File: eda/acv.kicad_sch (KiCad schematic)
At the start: 0 parts

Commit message: Add OBD2 connector symbol and footprint
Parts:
- added J1: ~, symbol acv:OBD2_J1962_MALE_90
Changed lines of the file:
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@@
 	(generator_version "9.0")
 	(paper "A4")
+	(symbol
+		(lib_id "acv:OBD2_J1962_MALE_90")
+		(at 88.9 63.5 0)
+		(unit 1)
+		(exclude_from_sim no)
+		(in_bom yes)
+		(on_board yes)
+		(dnp no)
+		(fields_autoplaced yes)
+		(property "Reference" "J1"
+			(at 107.95 63.4999 0)
+			(effects
+				(font
+					(size 1.27 1.27)
+				)
+				(justify left)
+			)
+		)
+		(property "Value" "~"
+			(at 107.95 66.0399 0)
+			(effects
+				(font
+					(size 1.27 1.27)
+				)
+				(justify left)
+			)
+		)
+		(property "Footprint" ""
+			(at 88.9 63.5 0)
+			(effects
+				(font
+					(size 1.27 1.27)
+				)
+				(hide yes)
+			)
+		)
+		(property "Datasheet" ""
+			(at 88.9 63.5 0)
+			(effects
+				(font
+					(size 1.27 1.27)
+				)
+				(hide yes)
+			)
+		)
+		(property "Description" ""
+			(at 88.9 63.5 0)
+			(effects
+				(font
+					(size 1.27 1.27)
+				)
+				(hide yes)
+			)
+		)
+		(pin "16"
+		)
+		(pin "9"
+		)
+		(pin "10"
+		)
+		(pin "15"
+		)
+		(pin "7"
+		)
+		(pin "6"
+		)
+		(pin "13"
+		)
+		(pin "5"
+		)
+		(pin "14"
+		)
+		(pin "12"
+		)
+		(pin "8"
+		)
+		(pin "4"
+		)
+		(pin "3"
+		)
+		(pin "11"
+		)
+		(pin "2"
+		)
+		(pin "1"
+		)
+		(instances
+			(project ""
+				(path "/b2ca9fb0-a35f-4499-b995-6512249a25c5"
+					(reference "J1")
+					(unit 1)
+				)
+			)
+		)
+	)
 	(sheet_instances
 		(path "/"

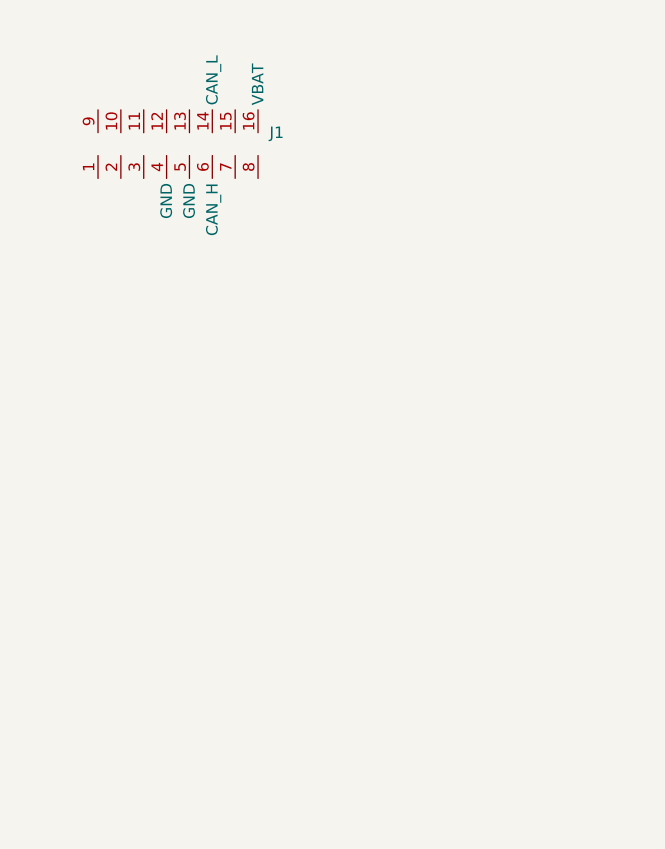
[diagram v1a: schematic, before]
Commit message: Add CAN transceiver symbol and footprint
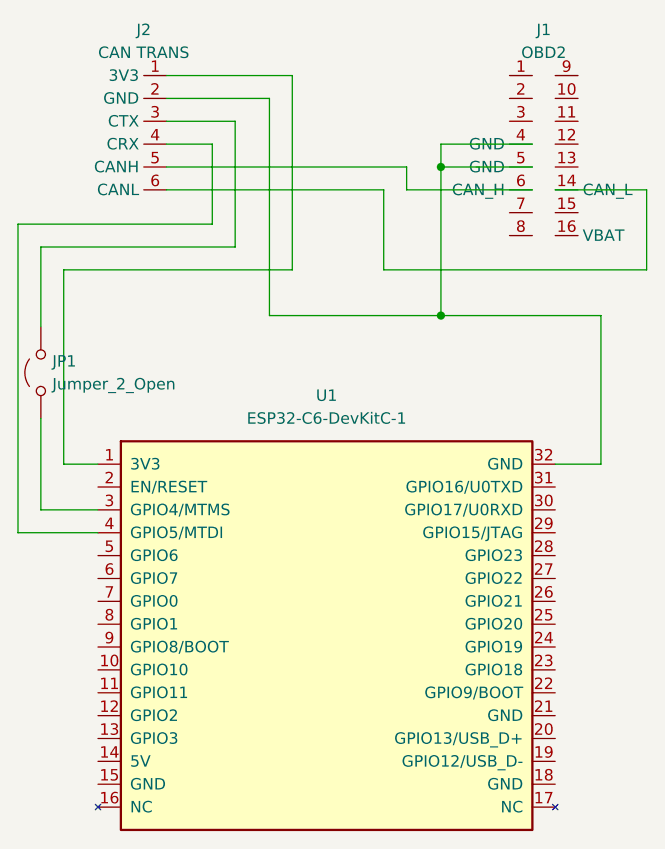
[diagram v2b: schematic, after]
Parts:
- added J2: CAN TRANS, symbol acv:SN65HVD230
- added JP1: Jumper_2_Open, symbol Jumper:Jumper_2_Open
- added U1: ESP32-C6-DevKitC-1, PCM_Espressif:ESP32-C6-DevKitC-1, symbol Espressif:ESP32-C6-DevKitC-1
- J1: value ~ -> OBD2
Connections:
- net at J1.14 (CAN_L): now also J2.6 (CANL)
- net at J1.4 (GND): now also J1.5 (GND), J2.2 (GND), U1.32 (GND)
- net at J1.6 (CAN_H): now also J2.5 (CANH)
- new net: J2.1 (3V3), U1.1 (3V3)
- new net: J2.3 (CTX), JP1.2 (B)
- new net: J2.4 (CRX), U1.4 (GPIO5/MTDI)
- new net: JP1.1 (A), U1.3 (GPIO4/MTMS)
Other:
- moved on the sheet: J1

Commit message: Add led and twai backend tasks
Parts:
- added D1: BLUE LED, symbol Device:LED
- added R1: 330ohm, symbol Device:R
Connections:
- net at J2.1 (3V3), U1.1 (3V3): now also R1.1
- net at U1.28 (GPIO23): now also D1.1 (K)
- new net: D1.2 (A), R1.2
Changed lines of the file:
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@@
 	(paper "A4")
+	(junction
+		(at 104.14 78.74)
+		(diameter 0)
+		(color 0 0 0 0)
+	)
 	(junction
 		(at 127 83.82)
@@
 	(wire
 		(pts
+			(xy 152.4 86.36) (xy 152.4 92.71)
+		)
+		(stroke
+			(width 0)
+			(type default)
+		)
+	)
+	(wire
+		(pts
 			(xy 139.7 100.33) (xy 144.78 100.33)
 		)
@@
 	(wire
 		(pts
+			(xy 139.7 110.49) (xy 152.4 110.49)
+		)
+		(stroke
+			(width 0)
+			(type default)
+		)
+	)
+	(wire
+		(pts
 			(xy 144.78 100.33) (xy 144.78 83.82)
 		)
@@
 	(wire
 		(pts
+			(xy 152.4 100.33) (xy 152.4 102.87)
+		)
+		(stroke
+			(width 0)
+			(type default)
+		)
+	)
+	(wire
+		(pts
 			(xy 137.16 64.77) (xy 127 64.77)
 		)
@@
 	(wire
 		(pts
+			(xy 104.14 78.74) (xy 110.49 78.74)
+		)
+		(stroke
+			(width 0)
+			(type default)
+		)
+	)
+	(wire
+		(pts
 			(xy 149.86 69.85) (xy 149.86 78.74)
 		)
@@
 	(wire
 		(pts
+			(xy 104.14 78.74) (xy 104.14 86.36)
+		)
+		(stroke
+			(width 0)
+			(type default)
+		)
+	)
+	(wire
+		(pts
 			(xy 88.9 100.33) (xy 85.09 100.33)
 		)
@@
 	(wire
 		(pts
+			(xy 104.14 86.36) (xy 152.4 86.36)
+		)
+		(stroke
+			(width 0)
+			(type default)
+		)
+	)
+	(wire
+		(pts
 			(xy 123.19 67.31) (xy 96.52 67.31)
 		)
@@
 	(wire
 		(pts
-			(xy 85.09 78.74) (xy 110.49 78.74)
+			(xy 85.09 78.74) (xy 104.14 78.74)
 		)
 		(stroke
@@
 			(width 0)
 			(type default)
+		)
+	)
+	(symbol
+		(lib_id "Device:LED")
+		(at 152.4 106.68 90)
+		(unit 1)
+		(exclude_from_sim no)
+		(in_bom yes)
+		(on_board yes)
+		(dnp no)
+		(fields_autoplaced yes)
+		(property "Reference" "D1"
+			(at 156.21 106.9974 90)
+			(effects
+				(font
+					(size 1.27 1.27)
+				)
+				(justify right)
+			)
+		)
+		(property "Value" "BLUE LED"
+			(at 156.21 109.5374 90)
+			(effects
+				(font
+					(size 1.27 1.27)
+				)
+				(justify right)
+			)
+		)
+		(property "Footprint" ""
+			(at 152.4 106.68 0)
+			(effects
+				(font
+					(size 1.27 1.27)
+				)
+				(hide yes)
+			)
+		)
+		(property "Datasheet" "~"
+			(at 152.4 106.68 0)
+			(effects
+				(font
+					(size 1.27 1.27)
+				)
+				(hide yes)
+			)
+		)
+		(property "Description" "Light emitting diode"
+			(at 152.4 106.68 0)
+			(effects
+				(font
+					(size 1.27 1.27)
+				)
+				(hide yes)
+			)
+		)
+		(property "Sim.Pins" "1=K 2=A"
+			(at 152.4 106.68 0)
+			(effects
+				(font
+					(size 1.27 1.27)
+				)
+				(hide yes)
+			)
+		)
+		(pin "1"
+		)
+		(pin "2"
+		)
+		(instances
+			(project ""
+				(path "/b2ca9fb0-a35f-4499-b995-6512249a25c5"
+					(reference "D1")
+					(unit 1)
+				)
+			)
 		)
 	)
@@
 					(unit 1)
 				)
+			)
+		)
+	)
+	(symbol
+		(lib_id "Device:R")
+		(at 152.4 96.52 0)
+		(unit 1)
+		(exclude_from_sim no)
+		(in_bom yes)
+		(on_board yes)
+		(dnp no)
+		(fields_autoplaced yes)
+		(property "Reference" "R1"
+			(at 154.94 95.2499 0)
+			(effects
+				(font
+					(size 1.27 1.27)
+				)
+				(justify left)
+			)
+		)
+		(property "Value" "330ohm"
+			(at 154.94 97.7899 0)
+			(effects
+				(font
+					(size 1.27 1.27)
+				)
+				(justify left)
+			)
+		)
+		(property "Footprint" ""
+			(at 150.622 96.52 90)
+			(effects
+				(font
+					(size 1.27 1.27)
+				)
+				(hide yes)
+			)
+		)
+		(property "Datasheet" "~"
+			(at 152.4 96.52 0)
+			(effects
+				(font
+					(size 1.27 1.27)
+				)
+				(hide yes)
+			)
+		)
+		(property "Description" "Resistor"
+			(at 152.4 96.52 0)
+			(effects
+				(font
+					(size 1.27 1.27)
+				)
+				(hide yes)
+			)
+		)
+		(pin "2"
+		)
+		(pin "1"
+		)
+		(instances
+			(project ""
+				(path "/b2ca9fb0-a35f-4499-b995-6512249a25c5"
+					(reference "R1")
+					(unit 1)
+				)

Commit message: Update EDA
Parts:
- removed D1: BLUE LED, symbol Device:LED
- removed J1: OBD2, symbol acv:OBD2_J1962_MALE_90
- removed J2: CAN TRANS, symbol acv:SN65HVD230
- removed JP1: Jumper_2_Open, symbol Jumper:Jumper_2_Open
- removed R1: 330ohm, symbol Device:R
- removed U1: ESP32-C6-DevKitC-1, PCM_Espressif:ESP32-C6-DevKitC-1, symbol Espressif:ESP32-C6-DevKitC-1
- added C1: EEE-FK1A471P, acv:EEHZT1E331UP, symbol acv:EEE-FK1A471P
- added C2: GCM188R71C104KA37D, CAPC1608X90N, symbol acv:GCM188R71C104KA37D
- added D1: SMBJ24A, acv:DIOM5436X261N, symbol acv:SMBJ24A
- added F1: SF-1206S150-2, acv:FUSC3116X70N, symbol acv:SF-1206S150-2
- added H1, H2, H3, H4: MountingHole, MountingHole:MountingHole_2.2mm_M2, symbol Mechanical:MountingHole
- added IC1: TJA1051T_3,118, acv:SOIC127P600X175-8N, symbol acv:TJA1051T_3,118
- added J1, J3: M20-7821646, acv:RHDR16W70P0X254_1X16_4104X250X850P, symbol acv:M20-7821646
- added J2: ~, acv:OBD2_J1962_MALE_90, symbol acv:OBD2_J1962_MALE_90
- added PS1: TSR_1-2450, TSR-1-24120, symbol acv:TSR_1-2450
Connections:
- new net: IC1.5 (VIO), J1.1
- new net: C1.1 (+), C2.1, IC1.3 (VCC), J1.14, PS1.3 (VOUT+)
- new net: IC1.1 (TXD), J1.3
- new net: IC1.4 (RXD), J1.4
- new net: F1.1, J2.16 (VBAT)
- new net: D1.1 (K), F1.2, PS1.1 (VIN+)
- new net: IC1.6 (CANL), J2.14 (CAN_L)
- new net: IC1.7 (CANH), J2.6 (CAN_H)
- new net GND: C1.2 (-), C2.2, D1.2 (A), IC1.2 (GND), IC1.8 (S), J1.15, J2.4 (GND), J2.5 (GND), J3.1, J3.12, J3.15, PS1.2 (GND)
